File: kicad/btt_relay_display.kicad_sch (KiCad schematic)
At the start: 15 parts, among them J1 RELAY, J2 PROGRAM, Q1 BC847, Q2 BC847, SW1 RESET

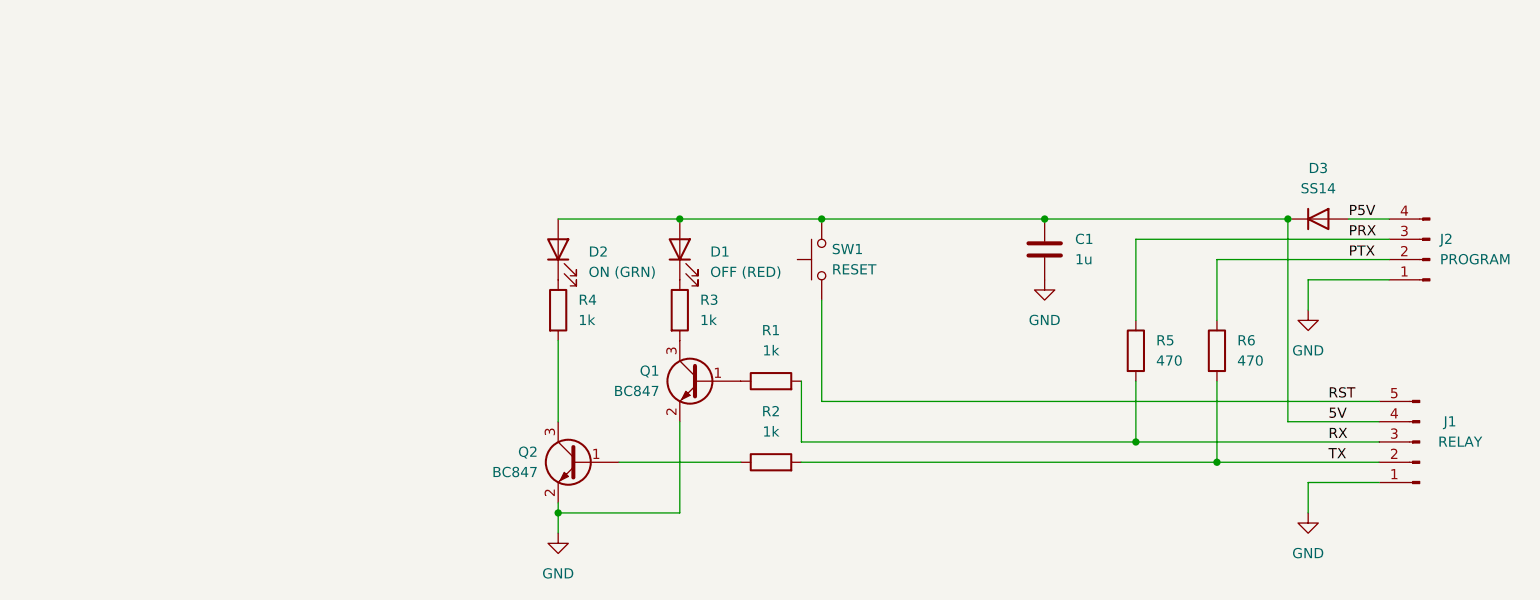
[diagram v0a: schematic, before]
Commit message: Holes made 2.5mm add pcb name text, generate gerbes for jlcpcb assembly service
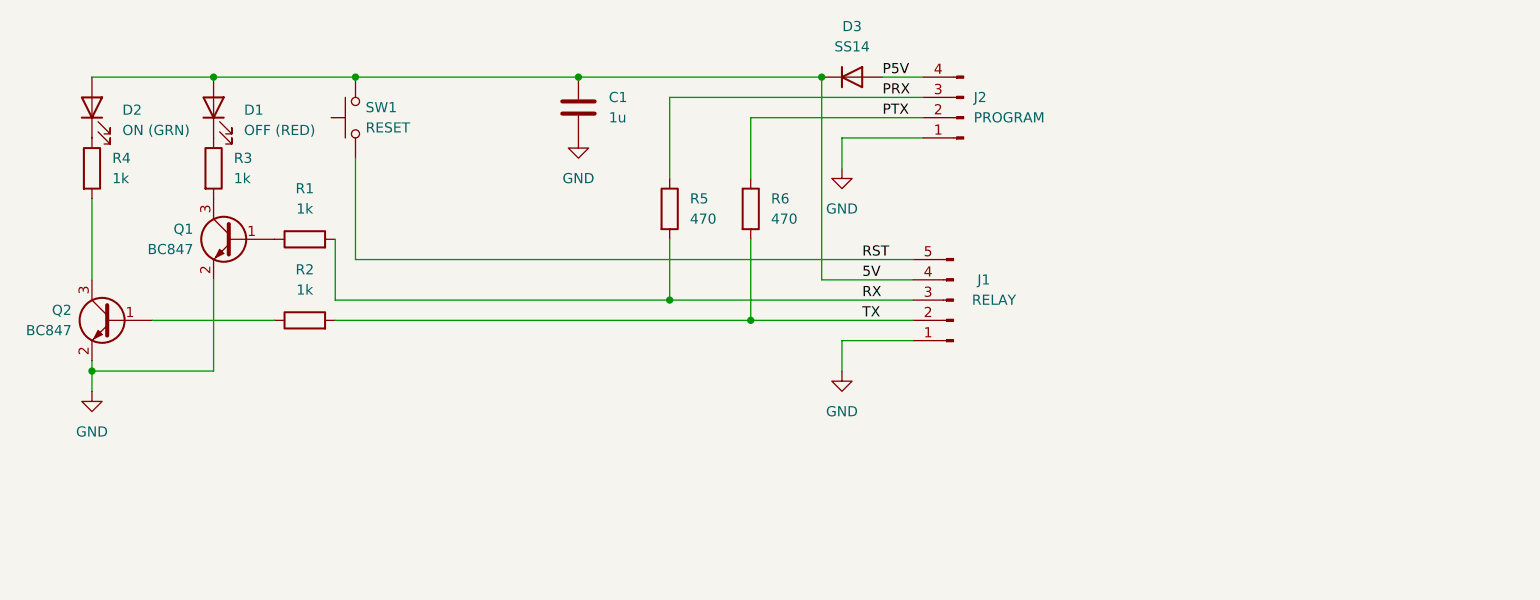
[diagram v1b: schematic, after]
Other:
- company: (none) -> ﻿CERN Open Hardware Licence v1.2 
- title: (none) -> BTT Relay Display
- moved on the sheet: C1, D1, D2, D3, J1, J2, Q1, Q2, R1, R2, R3, R4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
